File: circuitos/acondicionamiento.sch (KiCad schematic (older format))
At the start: 22 parts, among them Q1 BC547, U1 OPTO-TRANSISTOR-4, U2 LM358, U3 LM358

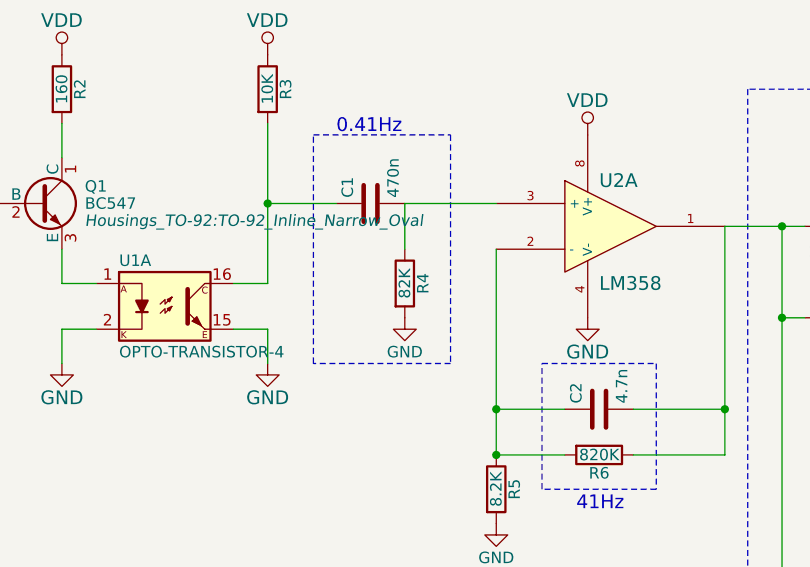
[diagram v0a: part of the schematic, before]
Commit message: Fix high-pass filter resistance vale
Was 82K instead of 820K
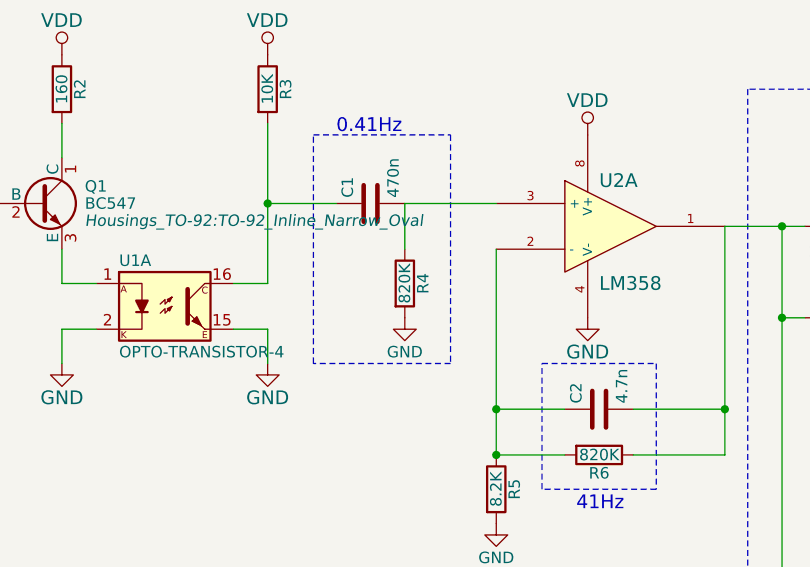
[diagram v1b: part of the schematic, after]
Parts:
- R4: value 82K -> 820K
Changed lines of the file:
@@
 P 3300 2550
 F 0 "R4" V 3380 2550 50  0000 C CNN
-F 1 "82K" V 3300 2550 50  0000 C CNN
+F 1 "820K" V 3300 2550 50  0000 C CNN
 F 2 "" V 3230 2550 30  0001 C CNN
 F 3 "" H 3300 2550 30  0000 C CNN
